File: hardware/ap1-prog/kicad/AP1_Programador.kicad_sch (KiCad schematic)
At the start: 41 parts, among them J1 BASE, J2 USB-C, J3 QWIIC, J4 EXT, SW1 MODO / BOOT, SW2 RESET, U1 ESP32-C3-WROOM-02, U2 AP63203WU, U3 USBLC6-2SC6, U4 TSOP38238

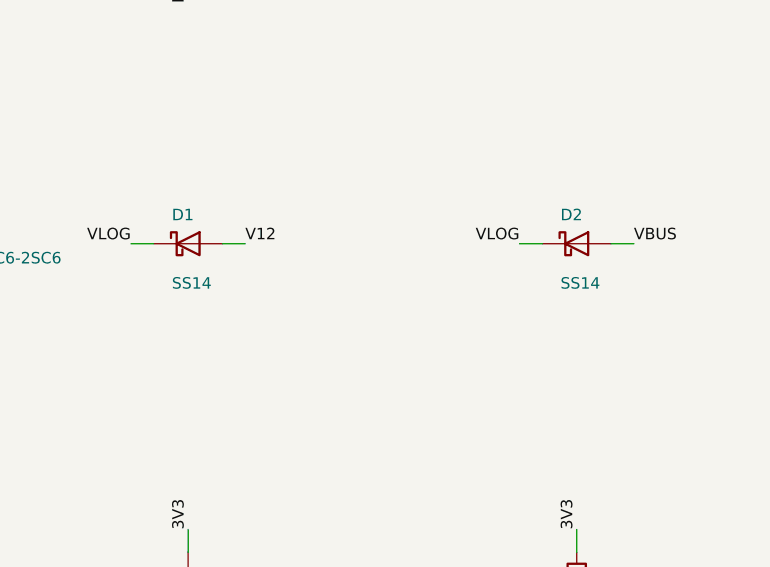
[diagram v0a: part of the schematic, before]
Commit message: AP-1 base a 4 capas, biblioteca JLCPCB y códigos LCSC automáticos
- placa.py: CAPAS=4 con planos internos (In1/In2 GND, tipo power para que
  Freerouting no rutee ahí), vías de costura GND (COSTURA) y zona sin cobre
  bajo la antena en todas las capas.
- AP1_Base: 4 capas JLC04161H-7628 (externas 2 oz, internas 1 oz), 61 vías de
  costura; ERC 0, DRC 0, 0 sin conectar, 0 diferencias.
- tools/jlcpcb.py + jlcpcb_catalogo.csv: 1499 piezas Basic/Preferred de la
  biblioteca JLCPCB-KiCad-Library (CDFER, MIT) y buscador por valor/huella.
- tools/descargar_biblioteca_jlcpcb.sh: instala la biblioteca para KiCad 9 y
  rehace el catálogo.
- salidas.py: BOM con LCSC y clase, RESUMEN_JLCPCB.txt con el cargo de piezas
  Extended, Gerber de todas las capas de cobre, PDF del lado inferior.
- Programador: D1/D2 SS14 -> B5819W (Preferred, misma huella).

Co-Authored-By: Claude Opus 5.5 <noreply@anthropic.com>
Claude-Session: https://claude.ai/code/session_01WVk3oGwfQfGTmAT2PMp8oW
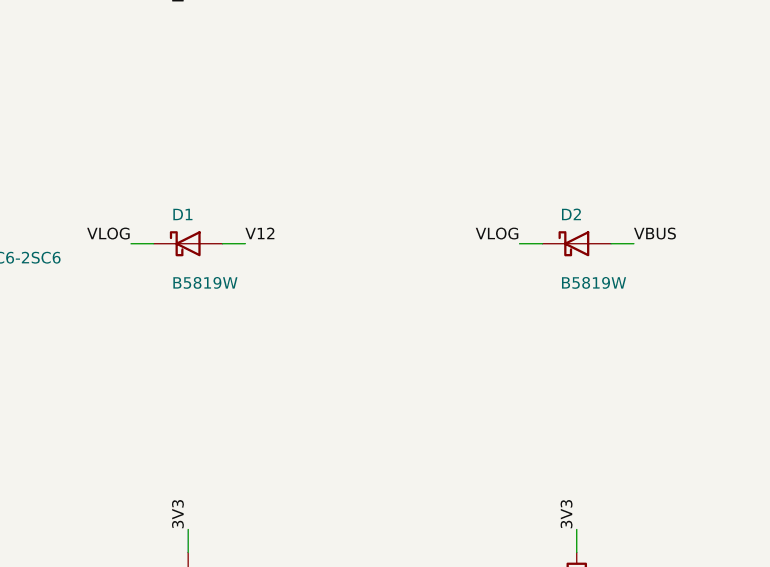
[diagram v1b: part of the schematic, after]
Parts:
- D1, D2: value SS14 -> B5819W
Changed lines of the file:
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@@
 			)
 		)
-		(property "Value" "SS14"
+		(property "Value" "B5819W"
 			(at 244.57 83.14 0)
 			(effects
@@
 			)
 		)
-		(property "Value" "SS14"
+		(property "Value" "B5819W"
 			(at 287.75 83.14 0)
 			(effects

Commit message: Pedido más económico en JLCPCB: menos piezas Extended y BOM solo SMD
- Base: memoria AT24CS02 -> M24C02 (Preferred). El programa crea el número
  de serie (128 bits al azar con la MAC del programador) si la memoria no trae.
- Programador y AP-0.2: botones TL3342 -> TS-1187A (Basic, misma huella).
  En la AP-0.2 se cambió la huella sin volver a rutear: DRC 0.
- Base: rutas fijas para SWC1/SWC2 y CC2 igual que CC1 (el canal 2 es
  copia del 1, 12.5 mm abajo). Ruteo estable: ERC 0, DRC 0, 0 sin conectar.
- salidas.py: BOM/CPL '_solo_SMD' para soldar a mano clemas y conectores,
  resumen con cargo por código LCSC distinto y costo de piezas Basic.
- jlcpcb.py: piezas reconocidas por huella (botones con valor de etiqueta).
- Cargo de montaje por pedido: base+programador de ~93 a ~84 USD, o ~54 USD
  en el pedido solo SMD.

Co-Authored-By: Claude Opus 5.5 <noreply@anthropic.com>
Claude-Session: https://claude.ai/code/session_01WVk3oGwfQfGTmAT2PMp8oW
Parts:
- SW1, SW2: footprint Button_Switch_SMD:SW_SPST_TL3342 -> Button_Switch_SMD:SW_Push_1P1T_XKB_TS-1187A
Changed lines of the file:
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@@
 	(title_block
 		(title "LetreroLab AP-1 - programador (ESP32-C3)")
-		(date "2026-10-01")
+		(date "2026-10-02")
 		(rev "1.0")
 		(company "PCB 52 x 42 mm, 2 capas")
@@
 			)
 		)
-		(property "Footprint" "Button_Switch_SMD:SW_SPST_TL3342"
+		(property "Footprint" "Button_Switch_SMD:SW_Push_1P1T_XKB_TS-1187A"
 			(at 289.56 40.64 0)
 			(hide yes)
@@
 			)
 		)
-		(property "Footprint" "Button_Switch_SMD:SW_SPST_TL3342"
+		(property "Footprint" "Button_Switch_SMD:SW_Push_1P1T_XKB_TS-1187A"
 			(at 30.48 78.74 0)
 			(hide yes)

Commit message: Listo para JLCPCB: códigos LCSC, reglas de fabricación y carpeta de pedido
- Códigos LCSC verificados para todas las piezas SMD (INA238, LMR16006,
  UCC27524, AL8860, TMP1075, MOSFET, bobinas, capacitor, fusible, módulo,
  conectores) en tools/jlcpcb.py; piezas reconocidas por huella.
- Shunt: el WSK2512 de 4 terminales se agotó en LCSC; base y AP-0.2 usan un
  HoJLR2512 1 mOhm 2 W (C2924520) con huella propia 'net tie' que conserva
  el sensado Kelvin (tools/huellas/LetreroLab.pretty).
- ESP32-C3-WROOM-02: huella propia con 4 vías de 0.3 mm en lugar de 12 de
  0.2 mm (proceso estándar de JLCPCB). Textos de serigrafía de 0.8 mm o más.
- IND: fusible de 3 A (el mismo de la base).
- AP-0.2 ruteada otra vez con el nuevo shunt.
- Las 4 placas: ERC 0, DRC 0, 0 sin conectar, 0 diferencias y 0 problemas
  con las reglas de fabricación de JLCPCB.
- PEDIDO_JLCPCB/ (+ .zip) con Gerber, BOM y CPL completos o solo SMD por
  placa, y PEDIDO_JLCPCB.md con las opciones exactas del pedido.

Co-Authored-By: Claude Opus 5.5 <noreply@anthropic.com>
Claude-Session: https://claude.ai/code/session_01WVk3oGwfQfGTmAT2PMp8oW
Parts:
- U1: footprint RF_Module:ESP32-C3-WROOM-02 -> LetreroLab:ESP32-C3-WROOM-02_JLC
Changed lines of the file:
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@@
 			)
 		)
-		(property "Footprint" "RF_Module:ESP32-C3-WROOM-02"
+		(property "Footprint" "LetreroLab:ESP32-C3-WROOM-02_JLC"
 			(at 30.48 40.64 0)
 			(hide yes)
